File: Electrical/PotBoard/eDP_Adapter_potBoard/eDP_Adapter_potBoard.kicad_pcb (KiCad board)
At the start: 2 copper layers, 28 x 22 mm, 6 parts, among them J1 Conn_01x05, M1 Standoff, M2 Standoff, M3 Standoff, U2 PotBoard

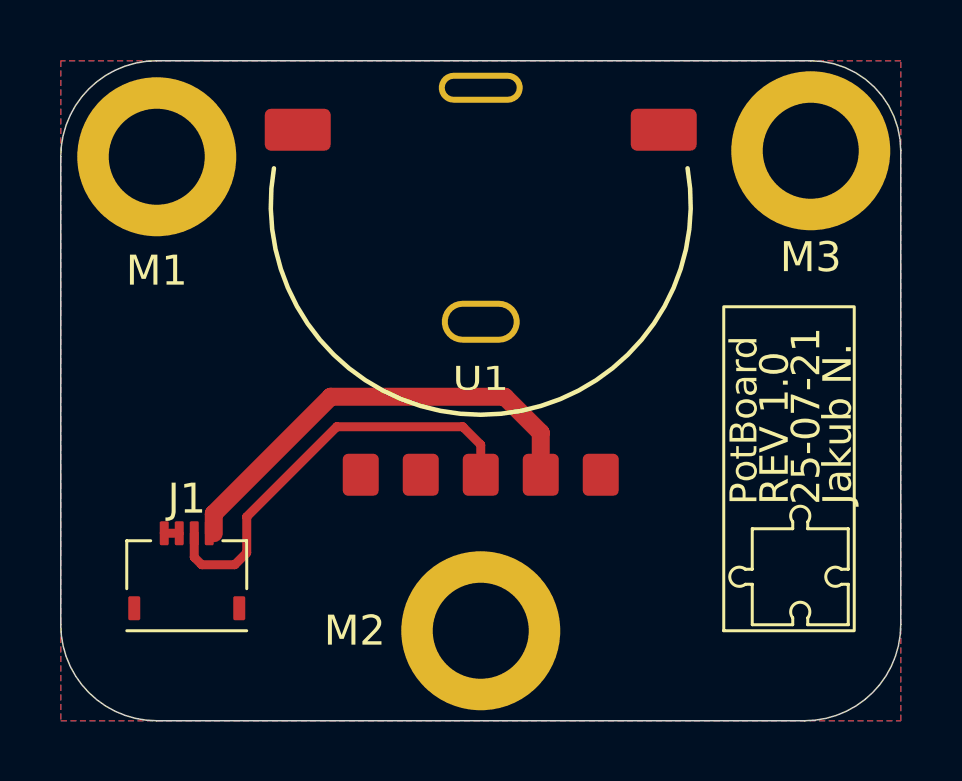
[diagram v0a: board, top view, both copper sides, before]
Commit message: BOM and fixed potboard font
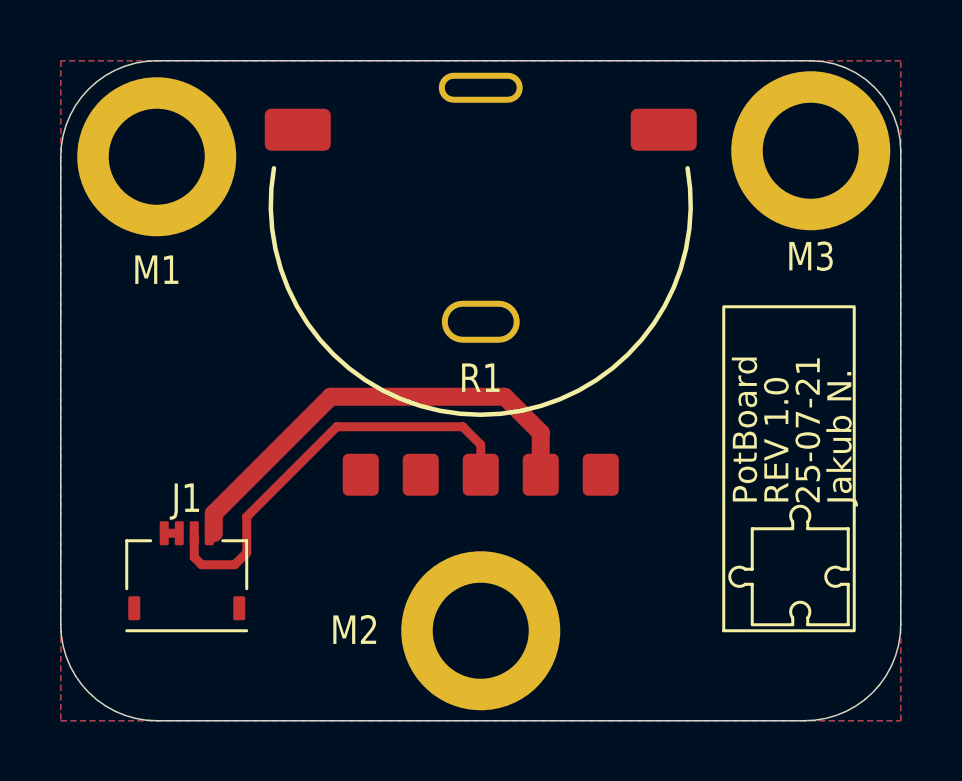
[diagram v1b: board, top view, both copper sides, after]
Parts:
- R1: renamed from U1; value ~ -> 5k
